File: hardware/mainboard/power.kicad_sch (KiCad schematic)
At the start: 19 parts, among them J1 Eurorack Power, U1 LD1117-3.3, U2 LM4040DBZ-10

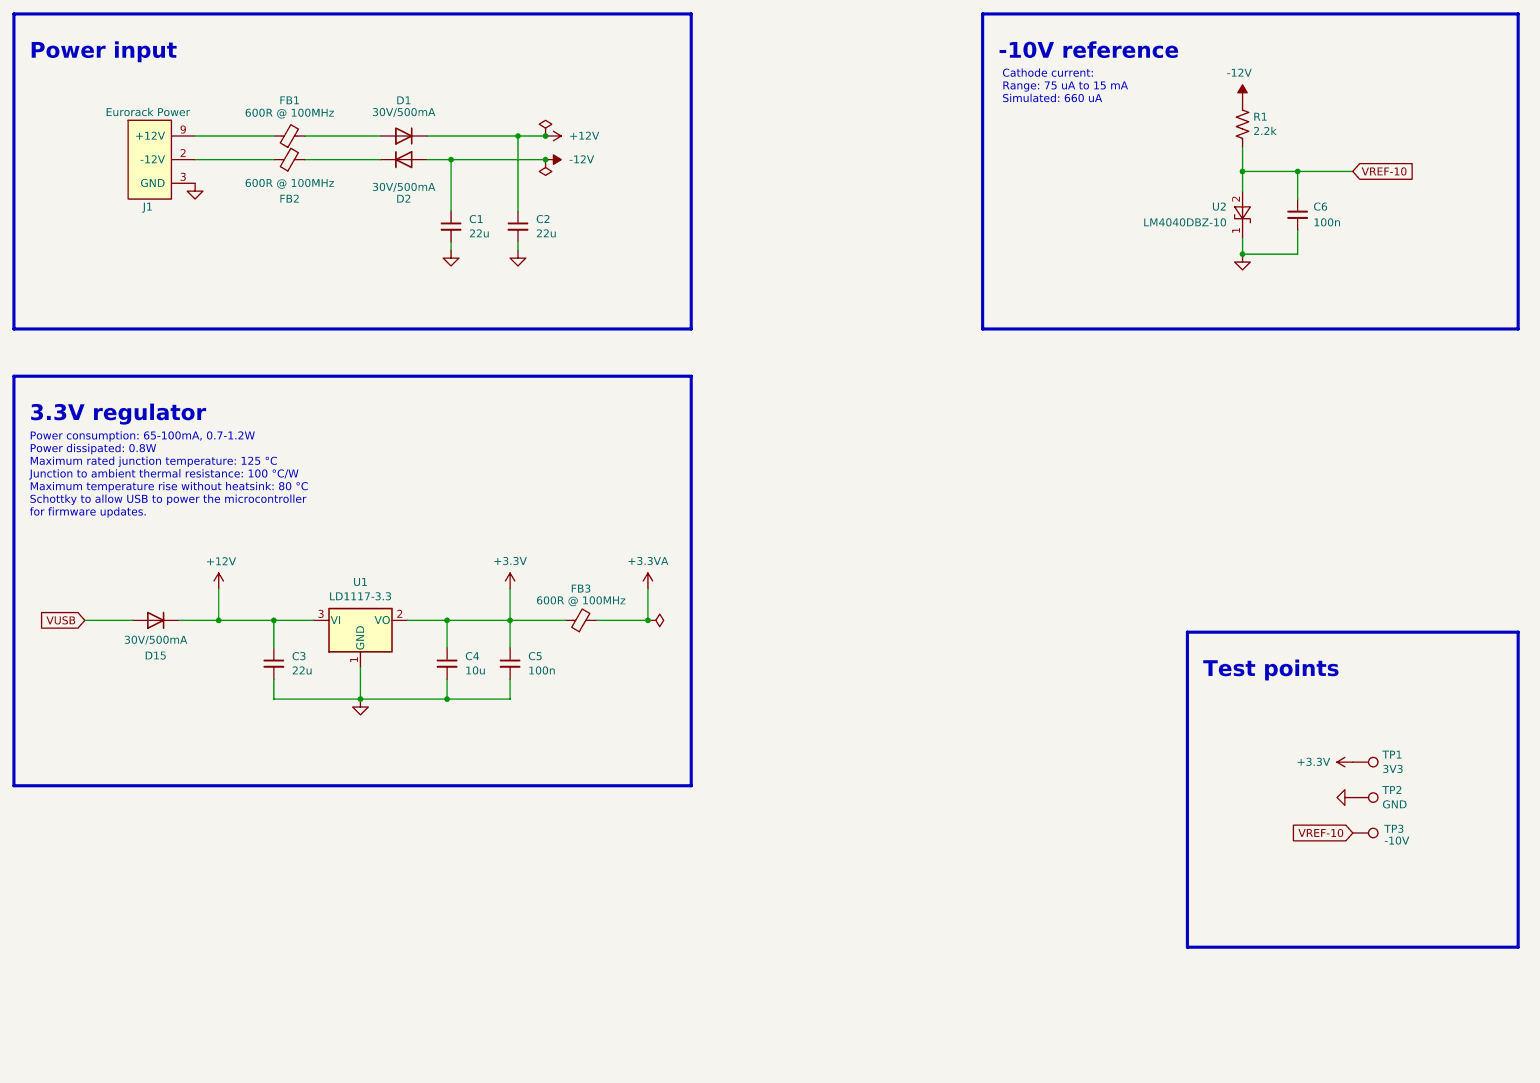
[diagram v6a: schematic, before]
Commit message: hardware: add rating field to schematic
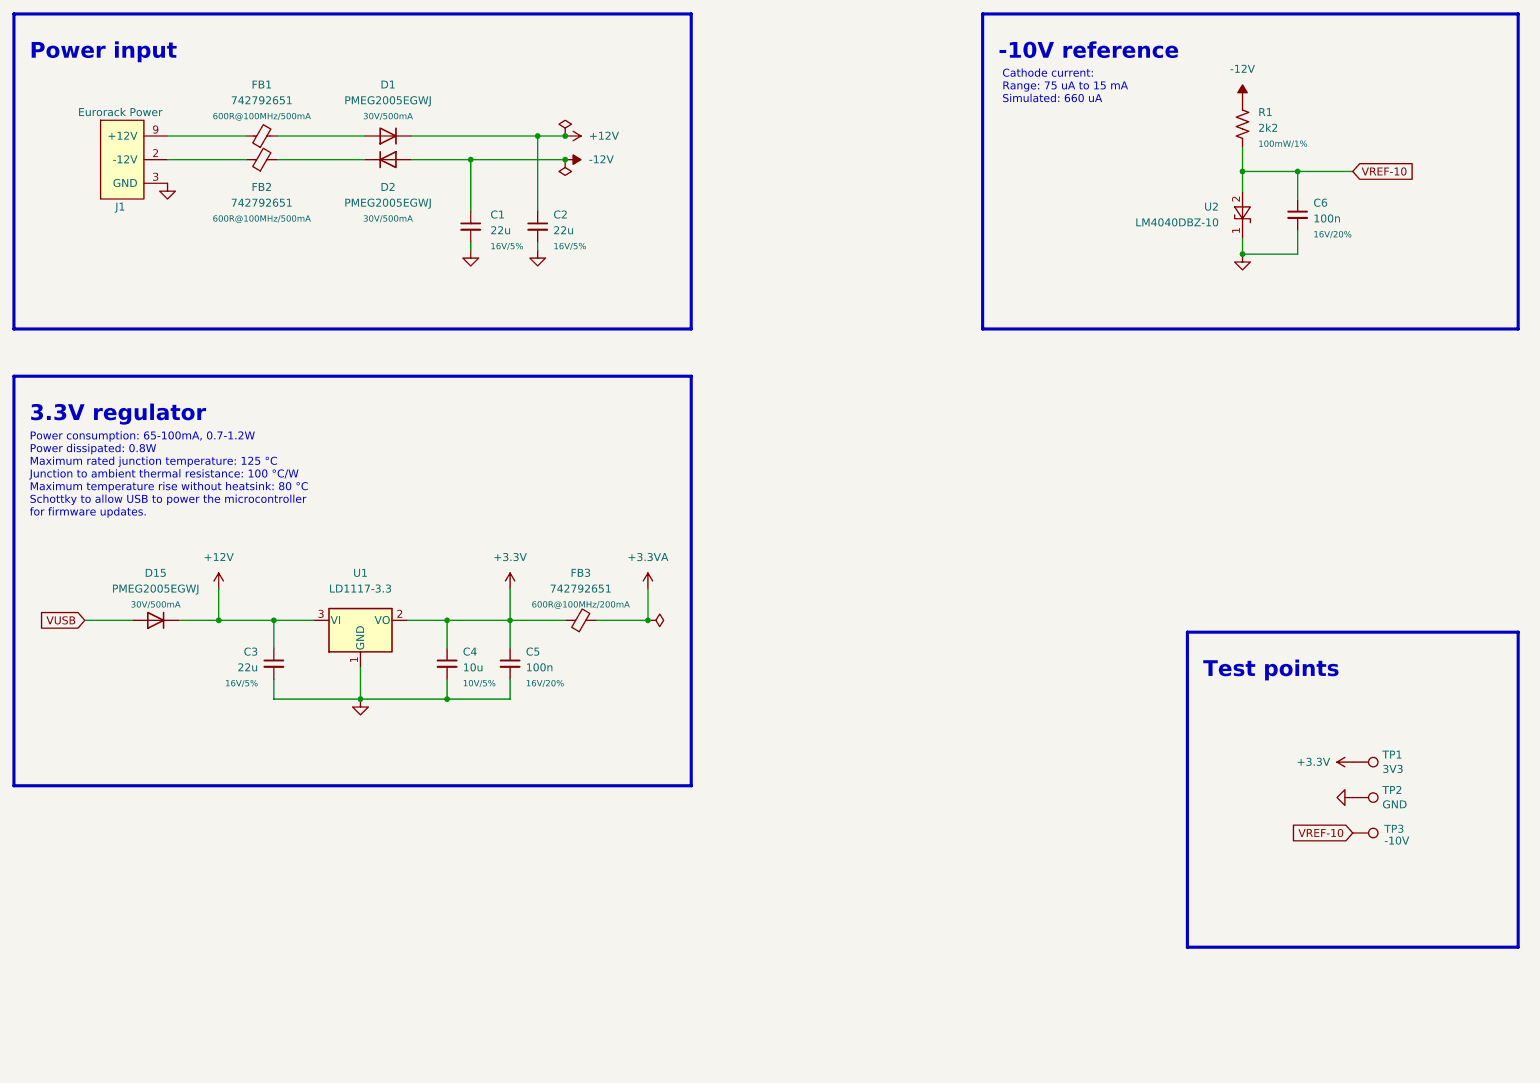
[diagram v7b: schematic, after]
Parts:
- C1, C2, C3: Rating (none) -> 16V/5%
- C4: Rating (none) -> 10V/5%
- C5, C6: Rating (none) -> 16V/20%
- D1, D15: value 30V/500mA -> PMEG2005EGWJ; Rating (none) -> 30V/500mA
- D2: value 30V/500mA -> PMEG2005EGWJ; Rating (none) -> 30V/500mA
- FB1, FB2: value 600R @ 100MHz -> 742792651; Rating (none) -> 600R@100MHz/500mA
- FB3: value 600R @ 100MHz -> 742792651; Rating (none) -> 600R@100MHz/200mA
- R1: value 2.2k -> 2k2; Rating (none) -> 100mW/1%
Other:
- moved on the sheet: C1, C2, D1, D2, FB1, FB2, J1

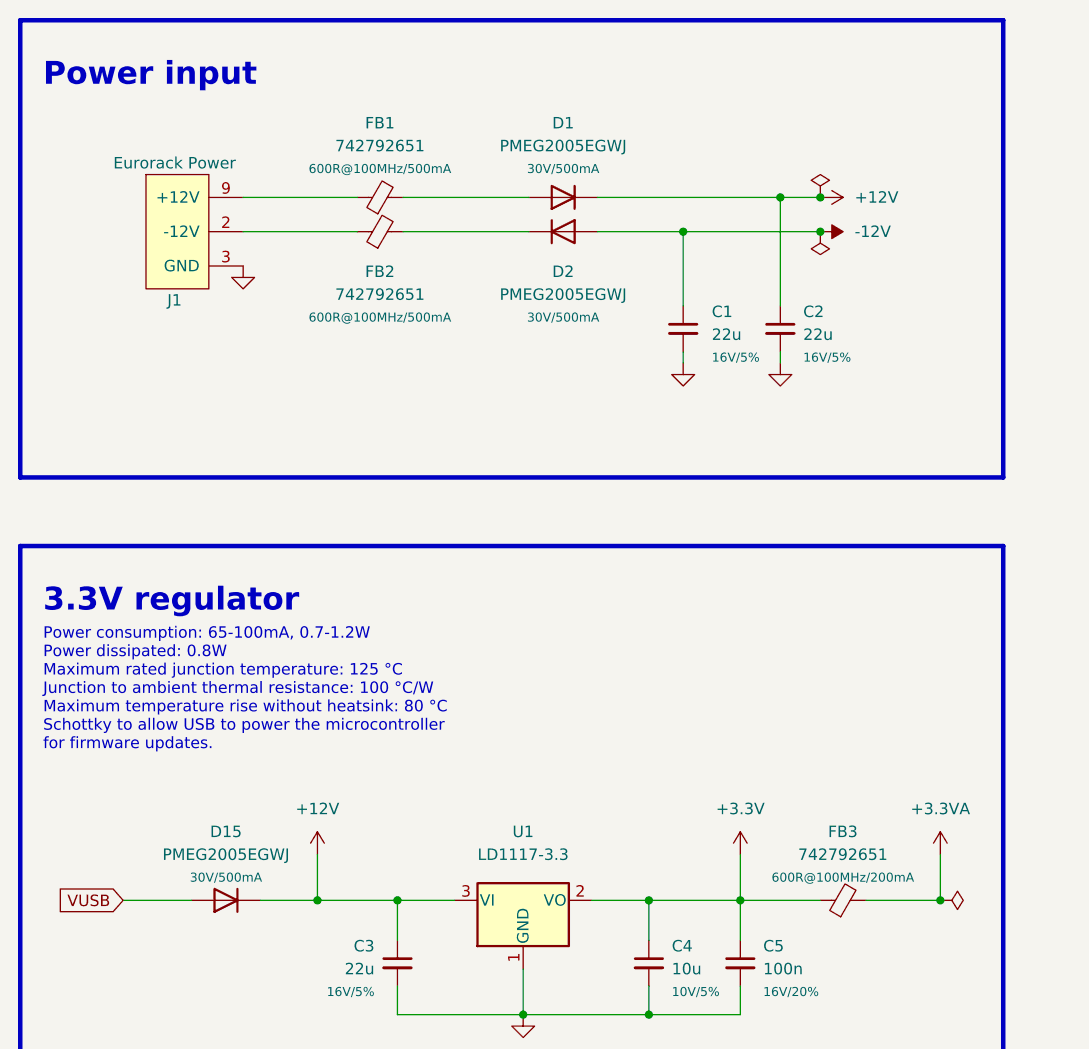
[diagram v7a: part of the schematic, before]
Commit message: hardware: fixup schematic fields
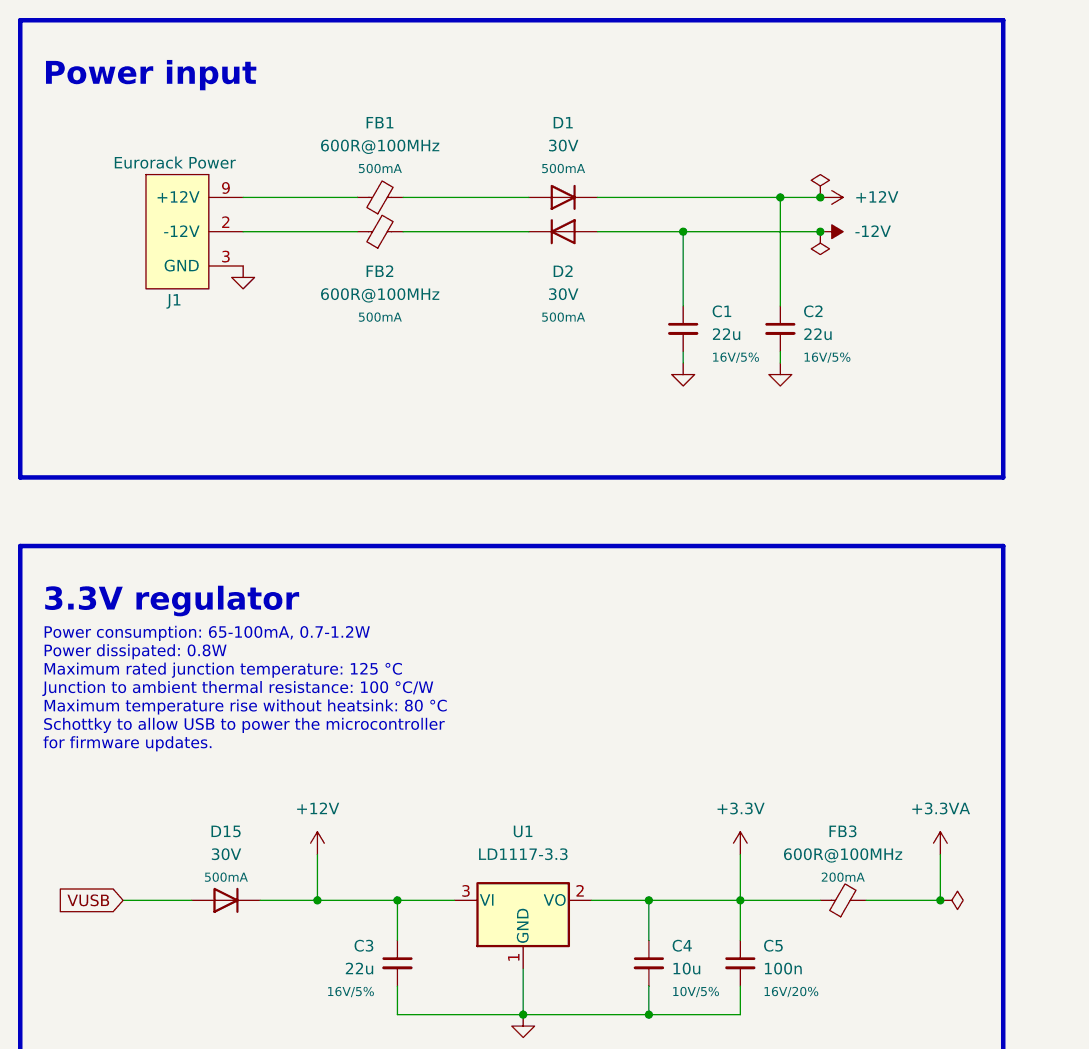
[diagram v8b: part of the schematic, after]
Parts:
- C1: MPN (none) -> CL21A226MAYNNNE; Notes (none) -> Bulk capacitance; Reqs Bulk capacitance, 16 V -> (none); finalized yes -> (none); mpn CL21A226MAYNNNE -> (none)
- C2: MPN (none) -> CL21A226MAYNNNE; Notes (none) -> Bulk capacitance; Reqs Board bulk capacitance, 16 V -> (none); finalized yes -> (none); mpn CL21A226MAYNNNE -> (none)
- C3: MPN (none) -> CL21A226MAYNNNE; Notes (none) -> Linear regulator input filter; Reqs Linear regulator input filter, 16 V -> (none); finalized yes -> (none); mpn CL21A226MAYNNNE -> (none)
- C4: MPN (none) -> CL10A106MP8NNNC; Notes (none) -> Linear regulator output filter; Reqs Linear regulator output filter, 10 V -> (none); finalized yes -> (none); mpn CL10A106MP8NNNC -> (none)
- C5, C6: MPN (none) -> CL05B104KO5NNNC; MacroFab MPN (none) -> MF-CAP-0402-0.1uF; Notes (none) -> Bypass; Reqs Bypass, 16 V -> (none); finalized yes -> (none); macrofab_mpn MF-CAP-0402-0.1uF -> (none); mpn CL05B104KO5NNNC -> (none)
- D1, D15, D2: value PMEG2005EGWJ -> 30V; MPN (none) -> PMEG2005EGWJ, PMEG3005EGWX; Rating 30V/500mA -> 500mA; finalized yes -> (none); mpn PMEG2005EGWJ, PMEG3005EGWX -> (none)
- FB1, FB2: value 742792651 -> 600R@100MHz; MPN (none) -> 742792651; Notes (none) -> Power filter; Rating 600R@100MHz/500mA -> 500mA; Reqs Power filter, 500mA DC current -> (none); finalized yes -> (none); mpn 742792651 -> (none)
- FB3: value 742792651 -> 600R@100MHz; MPN (none) -> 742792651; Notes (none) -> Analog power filter; Rating 600R@100MHz/200mA -> 200mA; Reqs Analog power filter, 200mA DC current -> (none); finalized yes -> (none); mpn 742792651 -> (none)
- J1: MPN (none) -> 4UCONN 20253, On-shore 302-S101; finalized yes -> (none); mpn 4UCONN 20253, On-shore 302-S101 -> (none)
- R1: MPN (none) -> ERJ-2RKF2201X; MacroFab MPN (none) -> MF-RES-0402-2K; Notes (none) -> -10V zener current control; Reqs -10V zener current control, 1%, 100 mW, thick film -> (none); macrofab_mpn MF-RES-0402-2K -> (none); mpn ERJ-2RKF2201X -> (none)
- TP1, TP2, TP3: DNP (none) -> 1; dnp 1 -> (none); finalized n/a -> (none)
- U1: MPN (none) -> LD1117DT33TR, AZ1117CD-3.3TRG1; finalized needs testing -> (none); mpn LD1117DT33TR, AZ1117CD-3.3TRG1 -> (none)
- U2: MPN (none) -> LM4040DIM3-10.0/NOPB; finalized yes -> (none); mpn LM4040DIM3-10.0/NOPB -> (none)
